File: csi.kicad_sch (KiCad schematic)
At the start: 38 parts, among them J6 Conn_FFC_WE_68715014522_ONE-S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, J7 Conn_FFC_WE_68715014022_ONE-S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, M1 Jetson-Nano-new-release, T8 BSS138PW, U4 PCA9547_VQFN

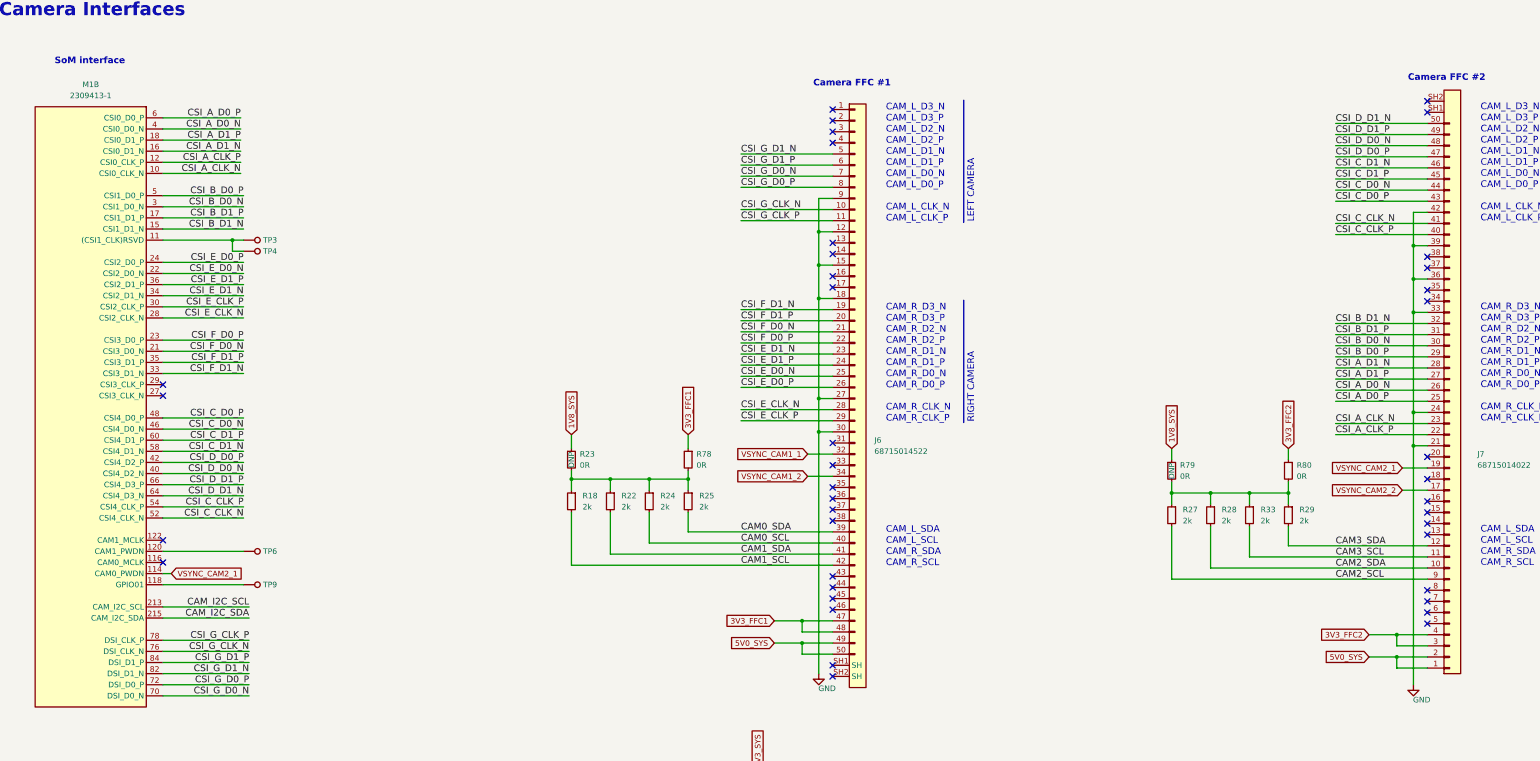
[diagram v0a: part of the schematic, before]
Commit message: [#56834] Fix components links
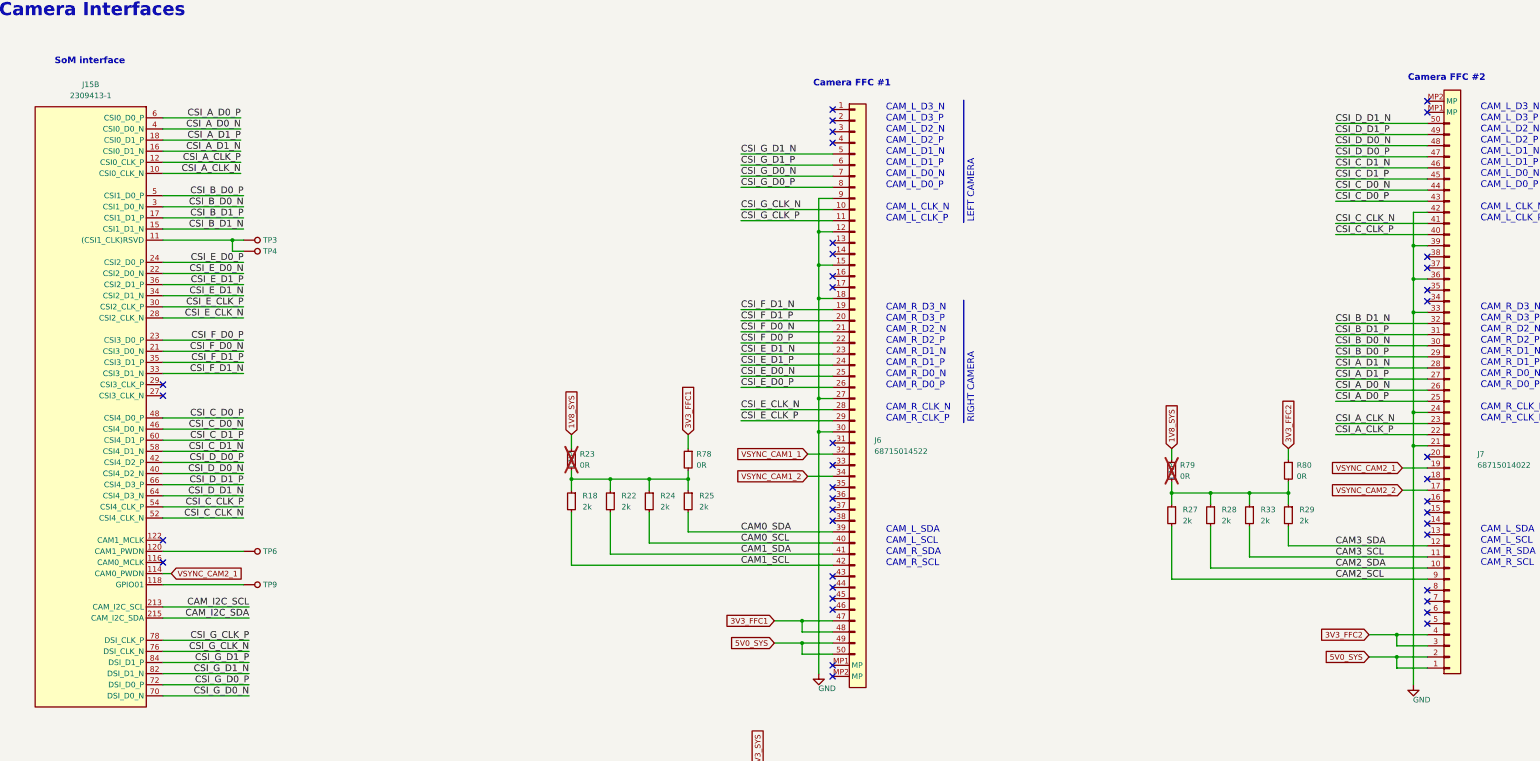
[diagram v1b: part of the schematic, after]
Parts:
- C9: footprint antmicro-footprints:C_0402_1005Metric -> jetson-nano-baseboard-footprints:C_0402_1005Metric; symbol antmicroCapacitors0402:C_100n_0402 -> jetson-nano-baseboard:C_100n_0402
- J15: renamed from M1; value Jetson-Nano-new-release -> Bus_DDR4_SODIMM_CUSTOM_Jetson-Nano-H9.2mm-socket; footprint antmicro-footprints:TE_2309413 -> jetson-nano-baseboard-footprints:TE_2309413; symbol antmicroSoMConnectors:Jetson-Nano-new-release -> jetson-nano-baseboard:Bus_DDR4_SODIMM_CUSTOM_Jetson-Nano-H9.2mm-socket
- J6: value Conn_FFC_WE_68715014522_ONE-SIDE -> Conn_FFC_WE_68715014522; footprint antmicro-footprints:Conn_FFC_WE_68715014x22 -> jetson-nano-baseboard-footprints:Conn_FFC_WE_68715014x22; symbol antmicroFCCConnectors:Conn_FFC_WE_68715014522_ONE-SIDE -> jetson-nano-baseboard:Conn_FFC_WE_68715014522; VSD_Class (none) -> Antmicro Dual Camera interface
- J7: value Conn_FFC_WE_68715014022_ONE-SIDE -> Conn_FFC_WE_68715014022; footprint antmicro-footprints:Conn_FFC_WE_68715014x22 -> jetson-nano-baseboard-footprints:Conn_FFC_WE_68715014x22; symbol antmicroFCCConnectors:Conn_FFC_WE_68715014022_ONE-SIDE -> jetson-nano-baseboard:Conn_FFC_WE_68715014022; MPN 68715014022 -> 68715014022
- R122: footprint antmicro-footprints:R_0402_1005Metric -> jetson-nano-baseboard-footprints:R_0402_1005Metric; symbol antmicroResistors0402:R_10k_0402 -> jetson-nano-baseboard:R_10k_0402
- R13, R15, R17, R19, R21, R57, R58, R59, R60, R61, R78, R80: footprint antmicro-footprints:R_0402_1005Metric -> jetson-nano-baseboard-footprints:R_0402_1005Metric; symbol antmicroResistors0402:R_0R_0402 -> jetson-nano-baseboard:R_0R_0402
- R18, R22, R24, R25, R27, R28, R29, R33, R34, R35: footprint antmicro-footprints:R_0402_1005Metric -> jetson-nano-baseboard-footprints:R_0402_1005Metric; symbol antmicroResistors0402:R_2k_0402 -> jetson-nano-baseboard:R_2k_0402
- R23, R79: footprint antmicro-footprints:R_0402_1005Metric -> jetson-nano-baseboard-footprints:R_0402_1005Metric; symbol antmicroResistors0402:R_0R_0402 -> jetson-nano-baseboard:R_0R_0402; now not fitted; now left out of the parts list
- R69: footprint antmicro-footprints:R_0402_1005Metric -> jetson-nano-baseboard-footprints:R_0402_1005Metric; symbol antmicroResistors0402:R_100k_0402 -> jetson-nano-baseboard:R_100k_0402
- T8: footprint antmicro-footprints:SC70-3 -> jetson-nano-baseboard-footprints:SC70-3; symbol antmicroTransistorsFETsMOSFETsSingle:BSS138PW -> jetson-nano-baseboard:BSS138PW
- TP1, TP10, TP3, TP4, TP6, TP9: footprint antmicro-footprints:TP_SMD_1.5mm -> jetson-nano-baseboard-footprints:TP_SMD_1.5mm; symbol antmicroTestPoints:TP_1.5mm_SMD -> jetson-nano-baseboard:TP_1.5mm_SMD; MPN N/A -> (none); Manufacturer N/A -> (none)
- U4: footprint antmicro-footprints:VQFN-24-1EP_3.8x3.8x1.0mm_P0.5mm -> jetson-nano-baseboard-footprints:VQFN-24-1EP_3.8x3.8x1.0mm_P0.5mm; symbol antmicroLogicSignalSwitchesMultiplexersDecoders:PCA9547_VQFN -> jetson-nano-baseboard:PCA9547_VQFN; MPN PCA9547BS,118 -> PCA9547BS,118

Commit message: [#57913] fix 2309413-1
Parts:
- C9: footprint jetson-nano-baseboard-footprints:C_0402_1005Metric -> antmicro-footprints:C_0402_1005Metric; symbol jetson-nano-baseboard:C_100n_0402 -> antmicroCapacitors0402:C_100n_0402
- J15: footprint jetson-nano-baseboard-footprints:TE_2309413 -> antmicro-footprints:TE_2309413; symbol jetson-nano-baseboard:Bus_DDR4_SODIMM_CUSTOM_Jetson-Nano-H9.2mm-socket -> antmicroSoMConnectors:Bus_DDR4_SODIMM_CUSTOM_Jetson-Nano-H9.2mm-socket
- J6: footprint jetson-nano-baseboard-footprints:Conn_FFC_WE_68715014x22 -> antmicro-footprints:Conn_FFC_WE_68715014x22; symbol jetson-nano-baseboard:Conn_FFC_WE_68715014522 -> antmicroFCCConnectors:Conn_FFC_WE_68715014522
- J7: footprint jetson-nano-baseboard-footprints:Conn_FFC_WE_68715014x22 -> antmicro-footprints:Conn_FFC_WE_68715014x22; symbol jetson-nano-baseboard:Conn_FFC_WE_68715014022 -> antmicroFCCConnectors:Conn_FFC_WE_68715014022
- R122: footprint jetson-nano-baseboard-footprints:R_0402_1005Metric -> antmicro-footprints:R_0402_1005Metric; symbol jetson-nano-baseboard:R_10k_0402 -> antmicroResistors0402:R_10k_0402
- R13, R15, R17, R19, R21, R23, R57, R58, R59, R60, R61, R78, R79, R80: footprint jetson-nano-baseboard-footprints:R_0402_1005Metric -> antmicro-footprints:R_0402_1005Metric; symbol jetson-nano-baseboard:R_0R_0402 -> antmicroResistors0402:R_0R_0402
- R18, R22, R24, R25, R27, R28, R29, R33, R34, R35: footprint jetson-nano-baseboard-footprints:R_0402_1005Metric -> antmicro-footprints:R_0402_1005Metric; symbol jetson-nano-baseboard:R_2k_0402 -> antmicroResistors0402:R_2k_0402
- R69: footprint jetson-nano-baseboard-footprints:R_0402_1005Metric -> antmicro-footprints:R_0402_1005Metric; symbol jetson-nano-baseboard:R_100k_0402 -> antmicroResistors0402:R_100k_0402
- T8: footprint jetson-nano-baseboard-footprints:SC70-3 -> antmicro-footprints:SC70-3; symbol jetson-nano-baseboard:BSS138PW -> antmicroTransistorsFETsMOSFETsSingle:BSS138PW
- TP1, TP10, TP3, TP4, TP6, TP9: footprint jetson-nano-baseboard-footprints:TP_SMD_1.5mm -> antmicro-footprints:TP_SMD_1.5mm; symbol jetson-nano-baseboard:TP_1.5mm_SMD -> antmicroTestPoints:TP_1.5mm_SMD
- U4: footprint jetson-nano-baseboard-footprints:VQFN-24-1EP_3.8x3.8x1.0mm_P0.5mm -> antmicro-footprints:VQFN-24-1EP_3.8x3.8x1.0mm_P0.5mm; symbol jetson-nano-baseboard:PCA9547_VQFN -> antmicroLogicSignalSwitchesMultiplexersDecoders:PCA9547_VQFN

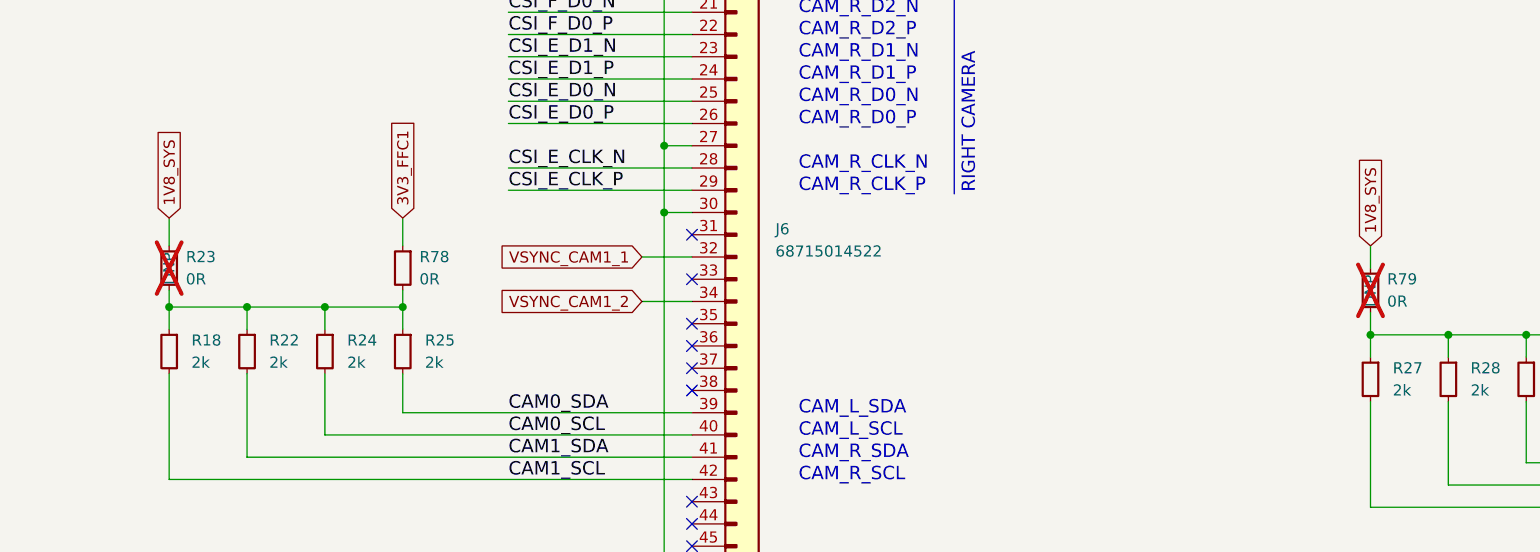
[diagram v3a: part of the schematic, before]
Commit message: [#83358] Run kmake dnp
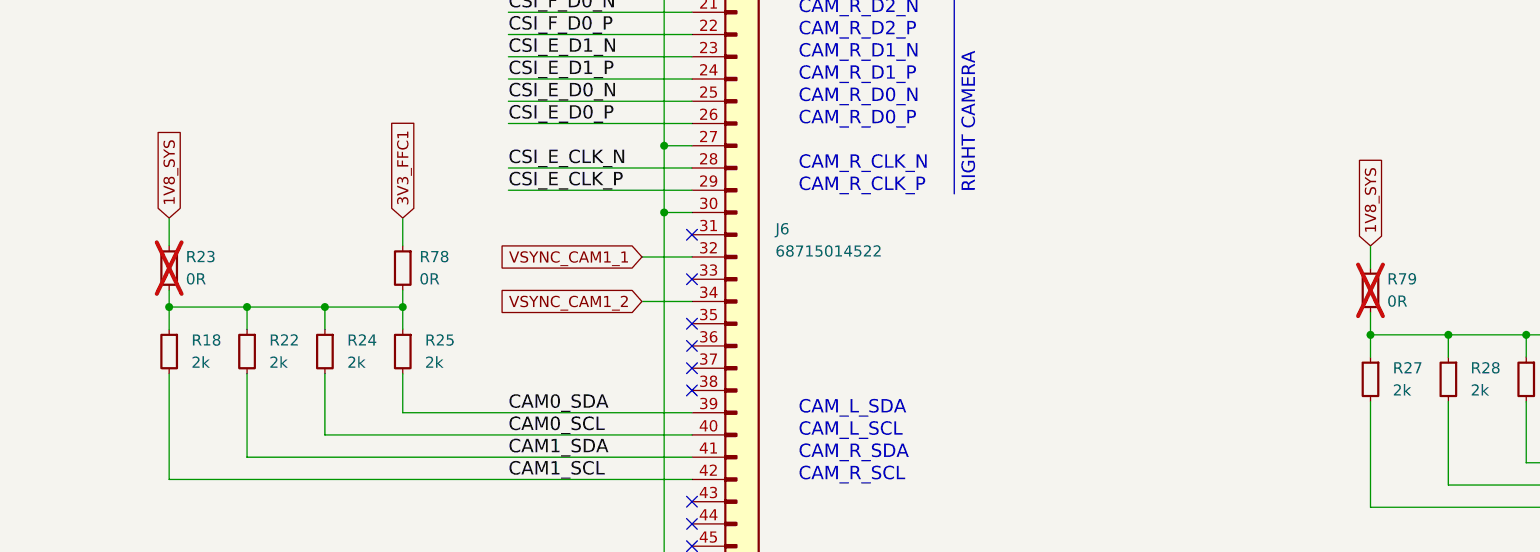
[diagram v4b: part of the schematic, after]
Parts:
- R23, R79: DNP DNP -> (none)
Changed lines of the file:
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@@
-			)
-		)
-		(property "DNP" "DNP"
-			(at 145.415 121.92 0)
-			(effects
-				(font
-					(size 1.27 1.27)
-				)
-				(justify right)
 			)
 		)
@@
 			(effects
 				(font
-					(size 1.27 1.27)
-				)
-				(justify right)
-			)
-		)
-		(property "DNP" "DNP"
-			(at 282.575 124.46 0)
-			(effects
-				(font
